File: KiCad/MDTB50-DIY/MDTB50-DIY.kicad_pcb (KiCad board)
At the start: 2 copper layers, 15.2 x 31.5 mm, 23 parts, among them U1 ICM-45686

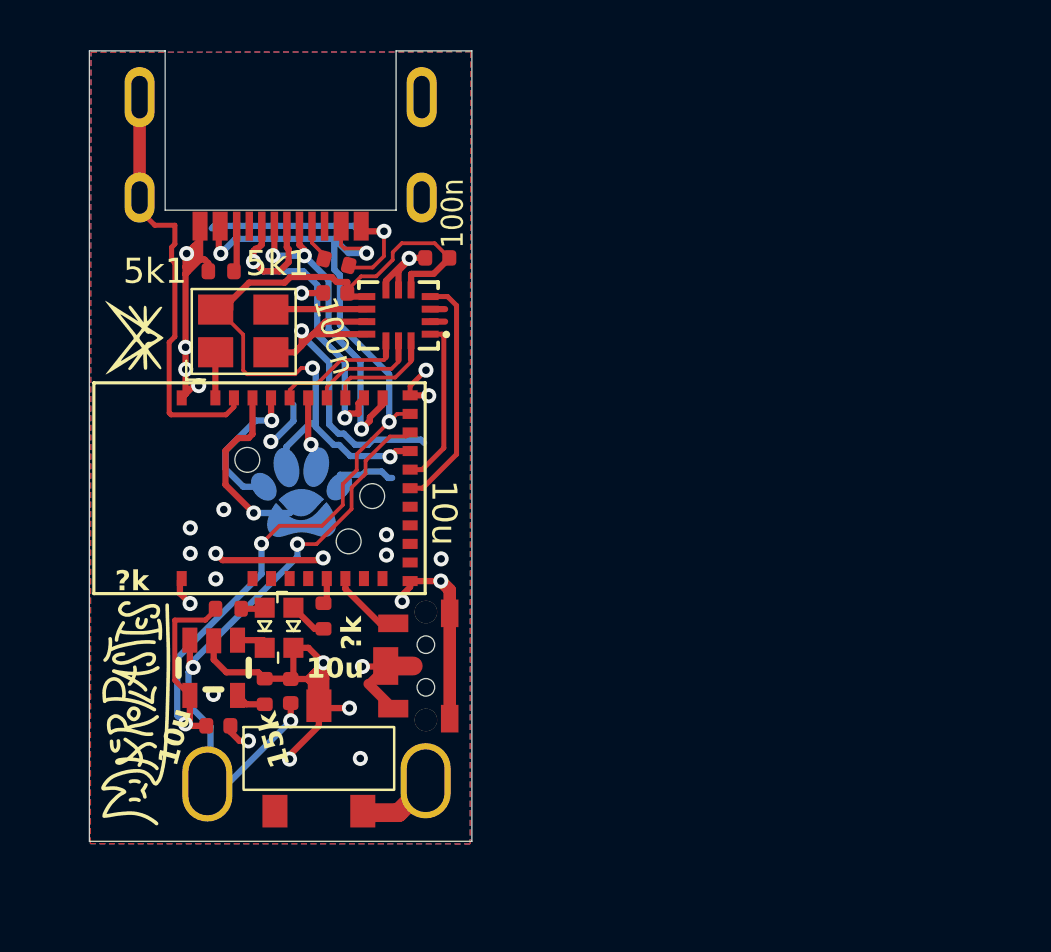
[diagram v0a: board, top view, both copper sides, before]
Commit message: - Added DIY pcb (unfinished) - Edited README.md
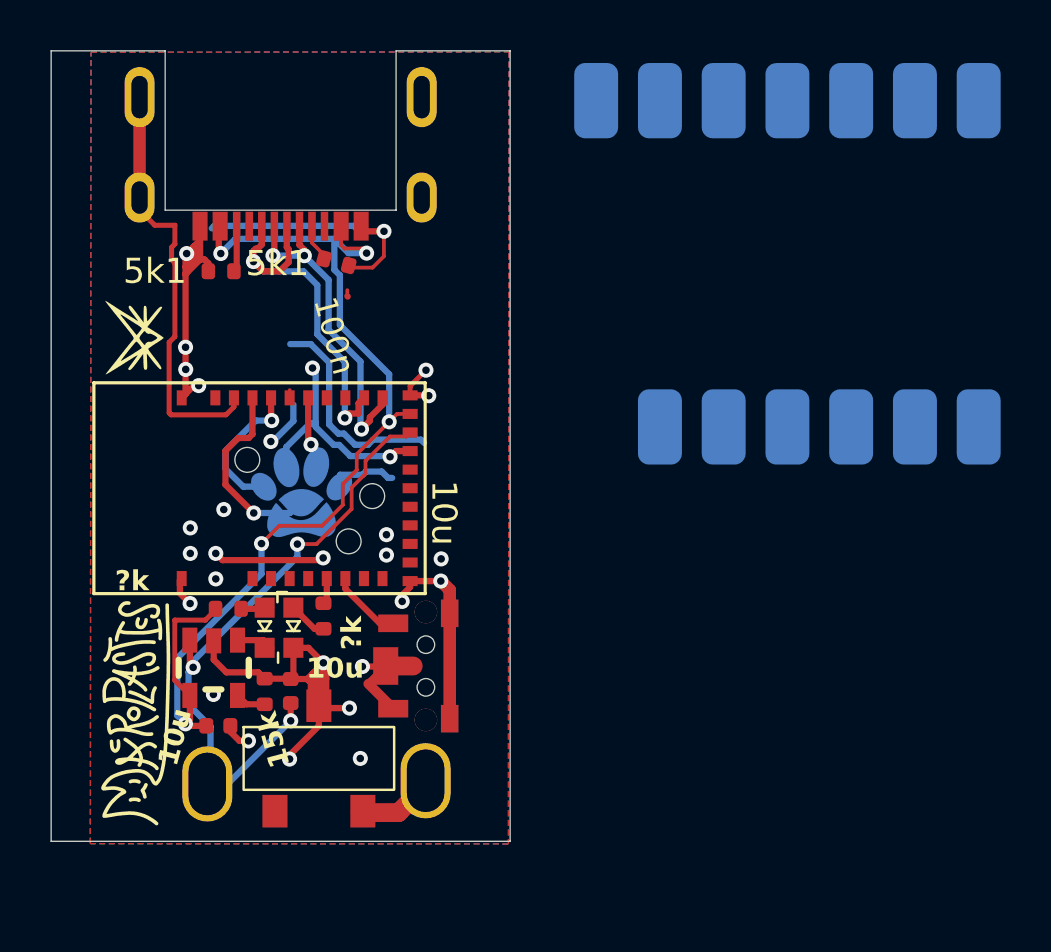
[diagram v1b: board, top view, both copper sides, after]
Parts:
- removed C1i1, C2i1: 100nf, passive_custom:C_0402_JLC
- removed U1: ICM-45686, imu_custom:ICM-42688-P
- removed U4: ~, oscillator_custom:HCI 1532H4-32K768JWPDTSNL
- added U6: ~, breakout_custom:kounolab-imu, B.Cu at (136.8, 72.1)
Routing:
- net +3.3V: track 30.2 -> 9.83 mm
- net GND: track 86.2 -> 74.5 mm, vias 30 -> 27
- net INT1: track 9.54 -> 0.00 mm
- net SDO: track 6.74 -> 0.00 mm
- net CS: track 5.37 -> 0.31 mm
- net SCL: track 4.54 -> 0.00 mm
- net SDA: track 4.40 -> 0.00 mm
- net CLK: track 4.34 -> 0.00 mm
- net CLK_EN: track 1.83 -> 0.00 mm
- net SDX: track 0.59 -> 0.00 mm
- net SCX: track 0.59 -> 0.00 mm
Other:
- board size 15.2 x 31.5 mm -> 18.3 x 31.5 mm

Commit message: - Started redoing layout for DIY variant
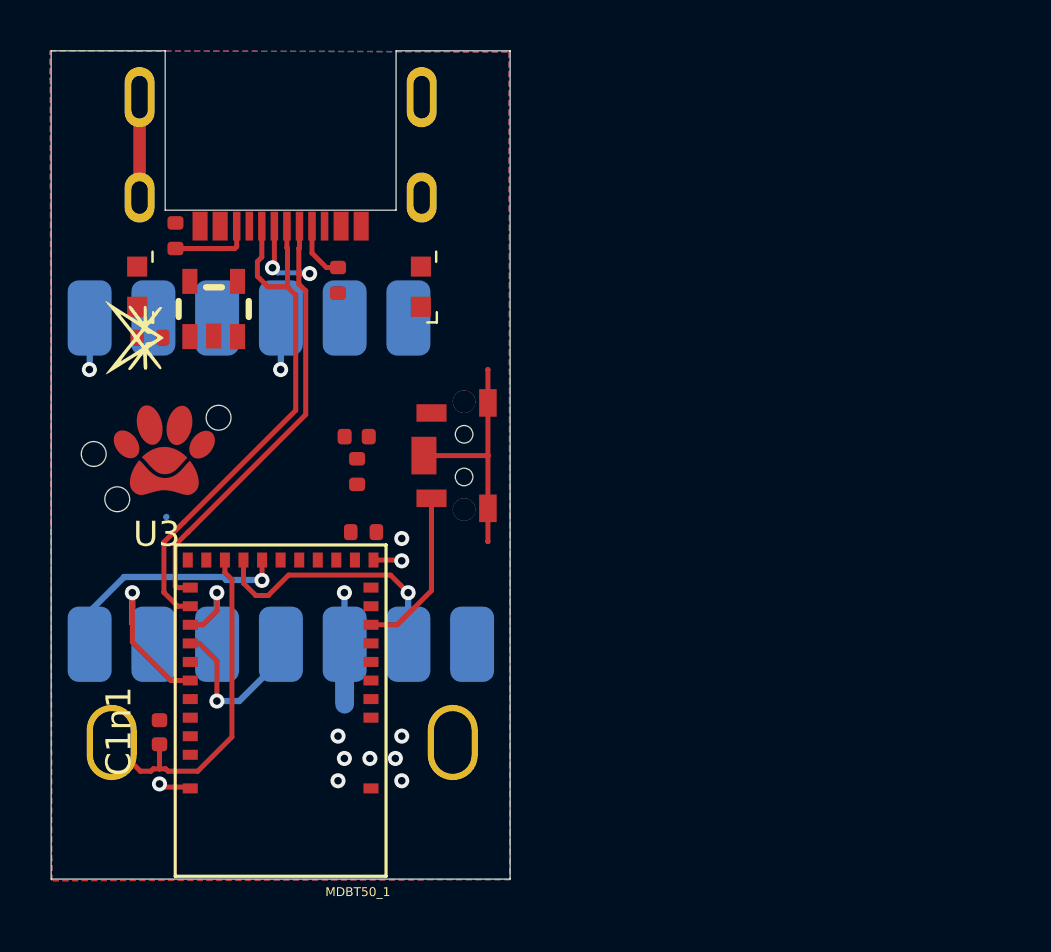
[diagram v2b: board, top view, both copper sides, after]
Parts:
- removed the G*** at (110.8, 89.8)
- removed U5: ~, Switch_Custom:CJS-1200TB
- U3: moved to F.Cu
- moved U6 21.7 mm to (116.6, 80.2), turned to 0 degrees
- moved LED1n1 14.5 mm to (122.2, 72.8), turned to -90 degrees
- moved LED1C1 14.5 mm to (110.9, 72.8), turned to -90 degrees
- moved ETA4054S1F1 14.3 mm to (113.9, 73.7), turned to -90 degrees
- moved C1C2 12.8 mm to (119.6, 78.7)
- moved R2C1 11.2 mm to (111.4, 74.8), turned to 180 degrees
- moved R1C1 9.51 mm to (119.6, 80.1), turned to -90 degrees
- moved MDBT50_1 8.90 mm to (116.6, 89.7), turned to 180 degrees
- moved S1 8.52 mm to (123.6, 79.5)
- moved U3 6.34 mm to (111.6, 79.6), turned to 0 degrees
- moved C1n1 5.48 mm to (111.8, 90.5)
- moved B+1 4.15 mm to (109.9, 90.9)
- moved R1n1 3.71 mm to (119.9, 82.6), turned to 180 degrees
- moved R2U1 2.31 mm to (112.4, 70.7), turned to -90 degrees
- moved B-1 1.87 mm to (123.4, 90.9)
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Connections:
- B-1 pad 1: Net-(B-1-Pad1) -> GND
- S1 pad 1: GND -> Net-(MDBT50_1-P0.31)
- S1 pad 2: Net-(MDBT50_1-P0.31) -> GND
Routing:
- net GND: track 74.5 -> 16.3 mm, vias 27 -> 11
- net VBUS: track 42.3 -> 0.00 mm, vias 5 -> 0
- net USB_CHASSIS: track 18.0 -> 5.55 mm
- net B+: track 24.8 -> 14.1 mm, vias 3 -> 0
- net SDO: track 0.00 -> 9.62 mm, vias 0 -> 1
- net SWCLK: track 7.82 -> 0.00 mm, vias 1 -> 0
- net D-: track 13.2 -> 21.0 mm, vias 3 -> 2
- net CS: track 0.31 -> 7.31 mm, vias 0 -> 1
- net D+: track 14.8 -> 21.6 mm, vias 2 -> 0
- net SCL: track 0.00 -> 6.79 mm, vias 0 -> 1
- net SWDIO: track 5.81 -> 0.00 mm, vias 1 -> 0
- net SDA: track 0.00 -> 4.07 mm, vias 0 -> 1
- net Net-(MDBT50_1-P0.31): track 2.89 -> 6.65 mm
- net Net-(B-1-Pad1): track 3.24 -> 0.00 mm
- net RST: track 2.94 -> 0.00 mm, vias 1 -> 0
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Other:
- board size 18.3 x 31.5 mm -> 18.3 x 33 mm
- board text removed: "100n"
- board text removed: "10u"
- board text removed: "15k"
- board text removed: "3V3"
- board text removed: "5k1"
- board text removed: "?k"
- board text removed: "GND"
- board text removed: "RST"
- board text removed: "SWCLK"
- board text removed: "SWDIO"

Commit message: - DIY PCB fully routed. But it kinda sucks.
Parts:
- added G***: LOGO, LOGO, F.Cu at (123.3, 94.6)
- moved G*** 19.8 mm to (109.7, 94.6), turned to 0 degrees
- moved R1C1 10.7 mm to (111.9, 72.7), turned to 90 degrees
- moved C1n1 9.65 mm to (116.2, 82.0), turned to 45 degrees
- moved R1n1 7.63 mm to (122.3, 75.3), turned to 90 degrees
- moved C1C2 5.96 mm to (116.1, 74.0), turned to 90 degrees
- moved U3 1.09 mm to (110.6, 79.2), turned to -120 degrees
- moved R1U1 0.43 mm to (118.6, 72.8)
- moved R2U1 0.40 mm to (112.0, 70.8), turned to -135 degrees
- moved LED1C1 0.14 mm to (110.7, 72.8)
- moved LED1n1 0.13 mm to (122.3, 72.8)
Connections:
- U3 pad 6: unconnected-(U3-NC-Pad6) -> SWCLK
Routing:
- net VBUS: track 0.00 -> 28.9 mm, vias 0 -> 4
- net GND: track 16.3 -> 42.5 mm, vias 11 -> 22
- net USB_CHASSIS: track 5.55 -> 30.2 mm
- net CLK_EN: track 2.06 -> 20.1 mm
- net SWCLK: track 0.00 -> 16.5 mm
- net Net-(MDBT50_1-P0.30): track 0.00 -> 13.7 mm, vias 0 -> 2
- net +3.3V: track 10.4 -> 23.2 mm, vias 1 -> 3
- net B+: track 14.1 -> 26.2 mm, vias 0 -> 2
- net RST: track 0.00 -> 10.7 mm
- net SWDIO: track 0.00 -> 10.0 mm
- net INT1: track 2.06 -> 11.9 mm
- net Net-(ETA4054S1F1-STAT): track 0.00 -> 6.76 mm
- net CS: track 7.31 -> 4.60 mm
- net Net-(U2-CC2): track 3.29 -> 5.94 mm, vias 0 -> 2
- net Net-(ETA4054S1F1-ISET): track 0.00 -> 1.33 mm
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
